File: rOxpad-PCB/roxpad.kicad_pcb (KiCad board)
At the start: 2 copper layers, 66 x 53 mm, 8 parts

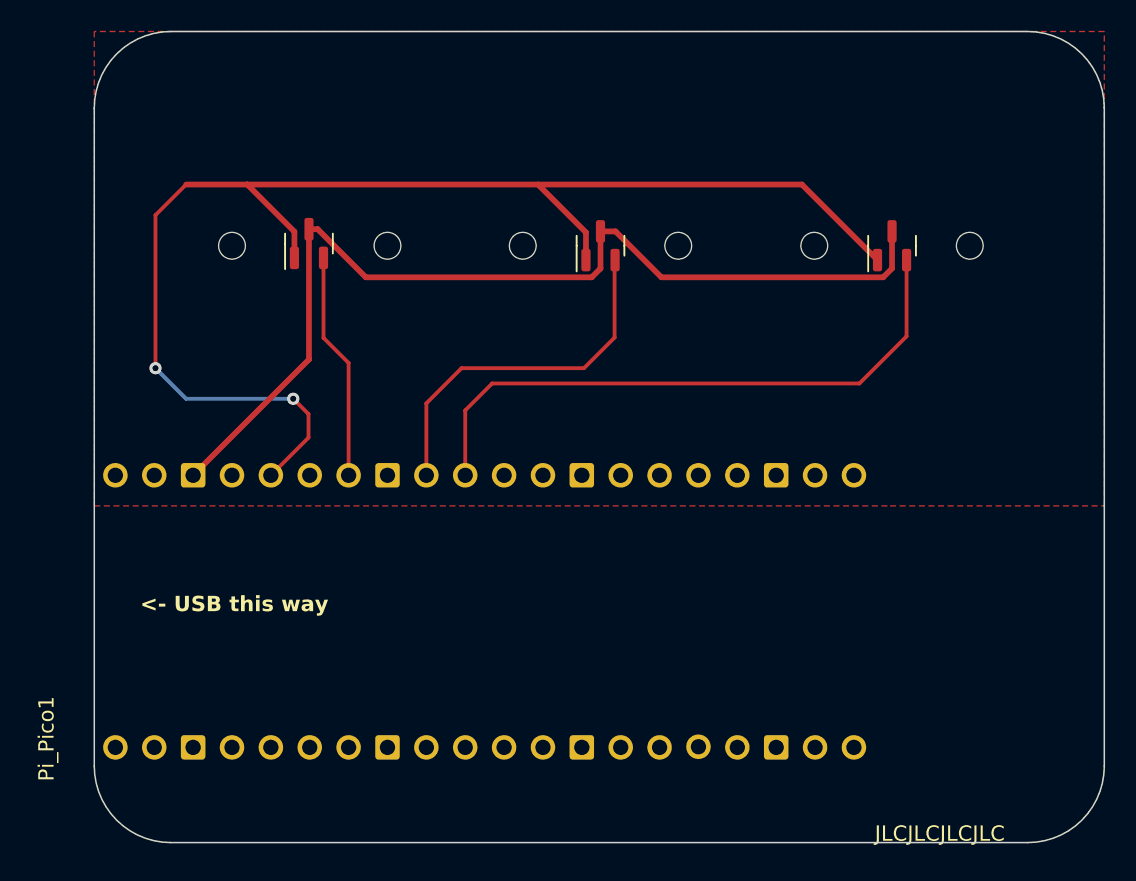
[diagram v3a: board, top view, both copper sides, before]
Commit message: change GND from seriees to paralel, and add support
Sucks because I had  already ordered the board, and recieved it, and soldered the pi pico. AAAAAAAAAAAAAAAAAAAAAAAAAAAAAAAAAAAAAAAAAAAAAAAAAAAAAAAAA
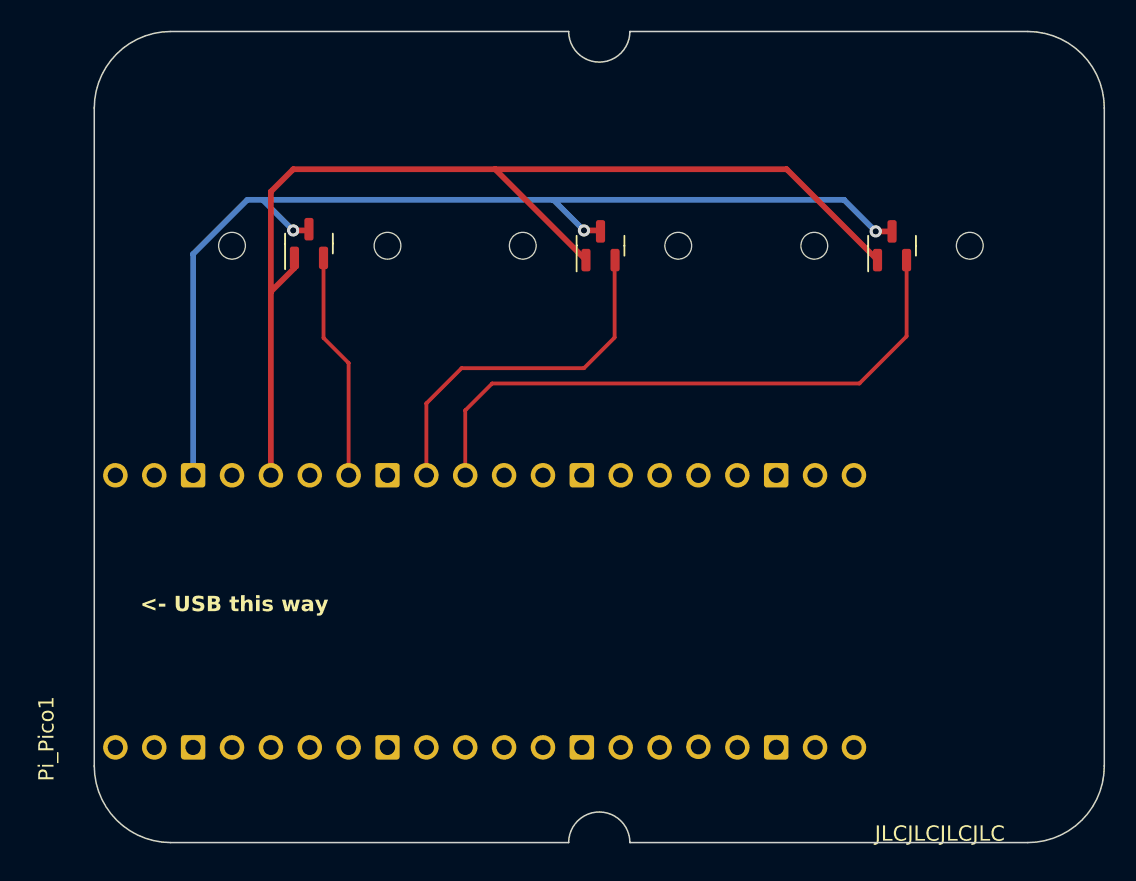
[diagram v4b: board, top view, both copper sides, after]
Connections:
- H1 pad 1: Net-(Left_sensor1-VDD) -> Net-(H1-VDD)
- H1 pad 2: Net-(Left_sensor1-OUT) -> Net-(H1-OUT)
- H1 pad 3: Net-(Left_sensor1-GND) -> Net-(H1-GND)
- H2 pad 1: Net-(Left_sensor1-VDD) -> Net-(H1-VDD)
- H2 pad 2: Net-(Middle_Sensor1-OUT) -> Net-(H2-OUT)
- H2 pad 3: Net-(Left_sensor1-GND) -> Net-(H1-GND)
- H3 pad 1: Net-(Left_sensor1-VDD) -> Net-(H1-VDD)
- H3 pad 2: Net-(Pi_Pico1-GP26) -> Net-(H3-OUT)
- H3 pad 3: Net-(Left_sensor1-GND) -> Net-(H1-GND)
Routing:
- net Net-(Left_sensor1-VDD): track 88.6 -> 0.00 mm, vias 2 -> 0
- net Net-(H1-VDD): track 0.00 -> 72.5 mm
- net Net-(H1-GND): track 0.00 -> 70.5 mm, vias 0 -> 3
- net Net-(Left_sensor1-GND): track 65.2 -> 0.00 mm
- net Net-(Pi_Pico1-GP26): track 40.1 -> 0.00 mm
- net Net-(H3-OUT): track 0.00 -> 40.1 mm
- net Net-(Middle_Sensor1-OUT): track 23.9 -> 0.00 mm
- net Net-(H2-OUT): track 0.00 -> 23.9 mm
- net Net-(Left_sensor1-OUT): track 14.9 -> 0.00 mm
- net Net-(H1-OUT): track 0.00 -> 14.9 mm
- removed copper zone on F.Cu, net Net-(H1-GND)
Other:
- outline, holes or cut-outs redrawn
- board text added: "___ /___ /___ - 1000 ___ /___ /___ - 2000 ___ /___ /___ - 3000 ___ /___ /___ - 4000 ___ /___ /___ - 5000 ___ /___ /___ - 6000"
- board text added: "no one can be good from the start - shige"
- board text added: "plz enjoy game -rrtyui"
- board text removed: "116"
- board text removed: "19/1/23"
- board text removed: "20/05/22 - 1000 05/10/22 - 2000 18/11/22 - 3000 25/12/23 - 4000 __ /__ /__ - 5000 __ /__ /__ - 6000"
- board text removed: "207"
- board text removed: "31/7/22"
- board text removed: "727"
- board text removed: "WYSI"

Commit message: fix keypad again and make it swag
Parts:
- moved H1 0.15 mm to (173.0, 58.0)
- moved REF** 0.08 mm to (173.0, 58.0)
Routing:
- net Net-(H1-GND): track 70.5 -> 6.27 mm
- net Net-(H1-VDD): track 72.5 -> 12.0 mm
- added copper zone on B.Cu, net Net-(H1-GND)
- added copper zone on F.Cu, net Net-(H1-VDD)
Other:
- board text added: "___ /___ /___ - 1000pp ___ /___ /___ - 2000pp ___ /___ /___ - 3000pp ___ /___ /___ - 4000pp ___ /___ /___ - 5000pp ___ /___ /___ - 6000pp"
- board text removed: "___ /___ /___ - 1000 ___ /___ /___ - 2000 ___ /___ /___ - 3000 ___ /___ /___ - 4000 ___ /___ /___ - 5000 ___ /___ /___ - 6000"

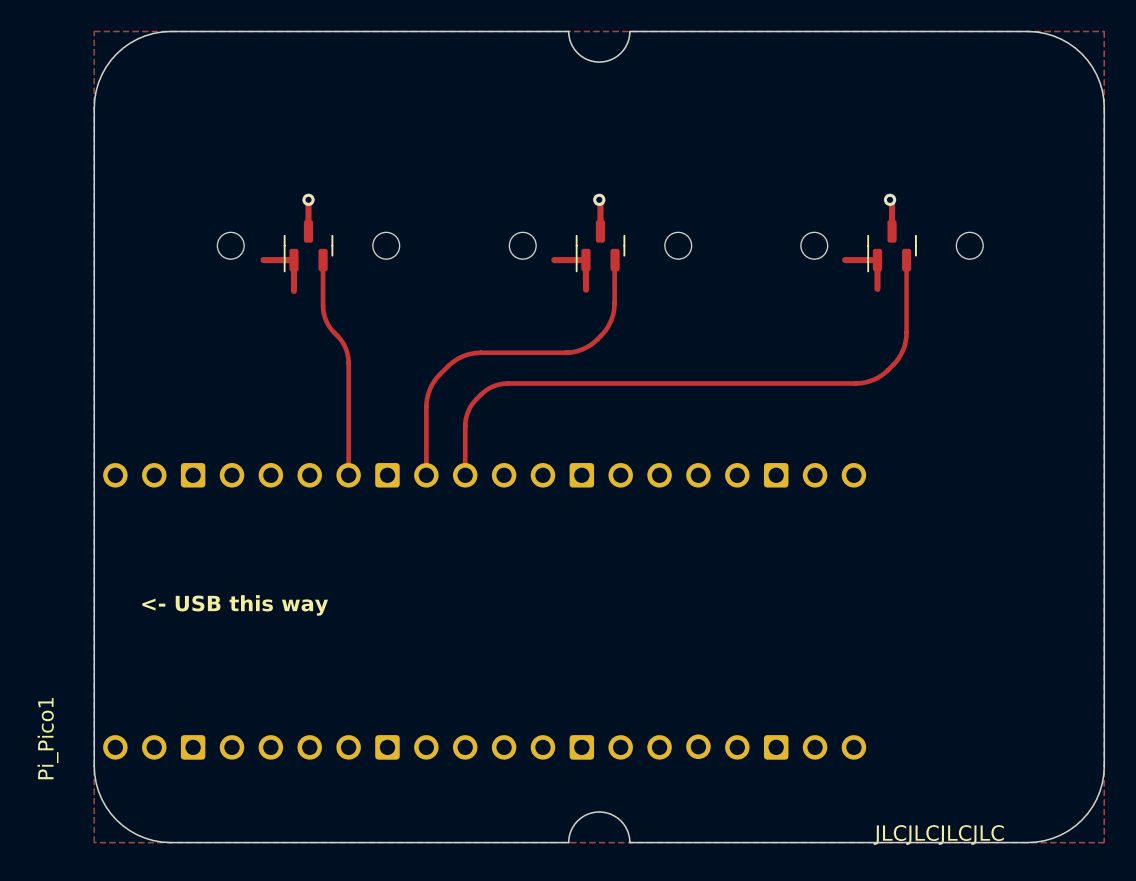
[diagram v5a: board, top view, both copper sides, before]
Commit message: changed gnd to agnd
I think this fixes it, won't check
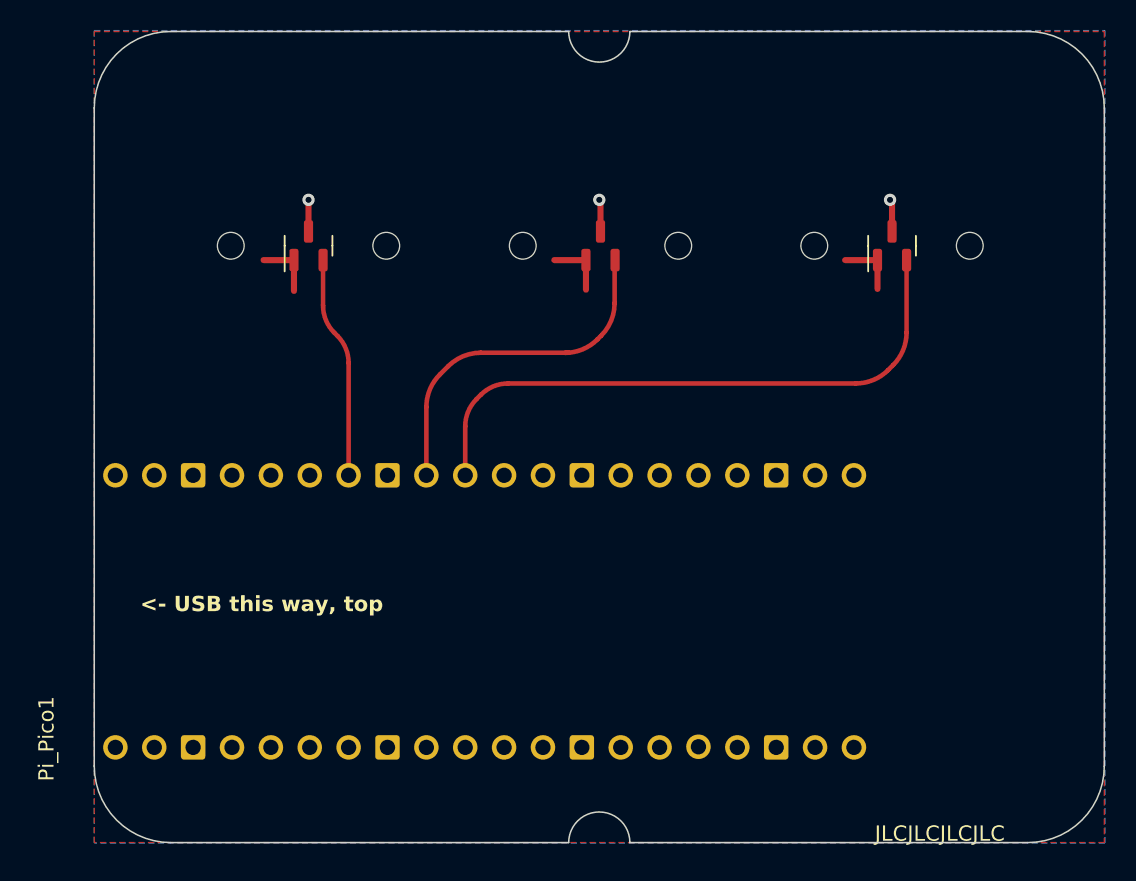
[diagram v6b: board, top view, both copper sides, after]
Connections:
- Pi_Pico1 pad 33: unconnected-(Pi_Pico1-AGND-Pad33) -> Net-(H1-GND)
- Pi_Pico1 pad 38: Net-(H1-GND) -> unconnected-(Pi_Pico1-GND-Pad38)
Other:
- board text added: "<- USB this way, top"
- board text removed: "<- USB this way"
